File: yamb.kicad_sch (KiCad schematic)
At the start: 18 parts, among them J1 Barrel_Jack, J2 I2C, J3 HEADER, J4 HEADER_2.54, J5 Remote_Reset, J6 Power_Switch, P1 USB_C_Plug_USB2.0, SW1 RESET, U1 TPS3808DBV, U2 MCSBC, U3 SVR, U4 RAK4630, U5 BME280

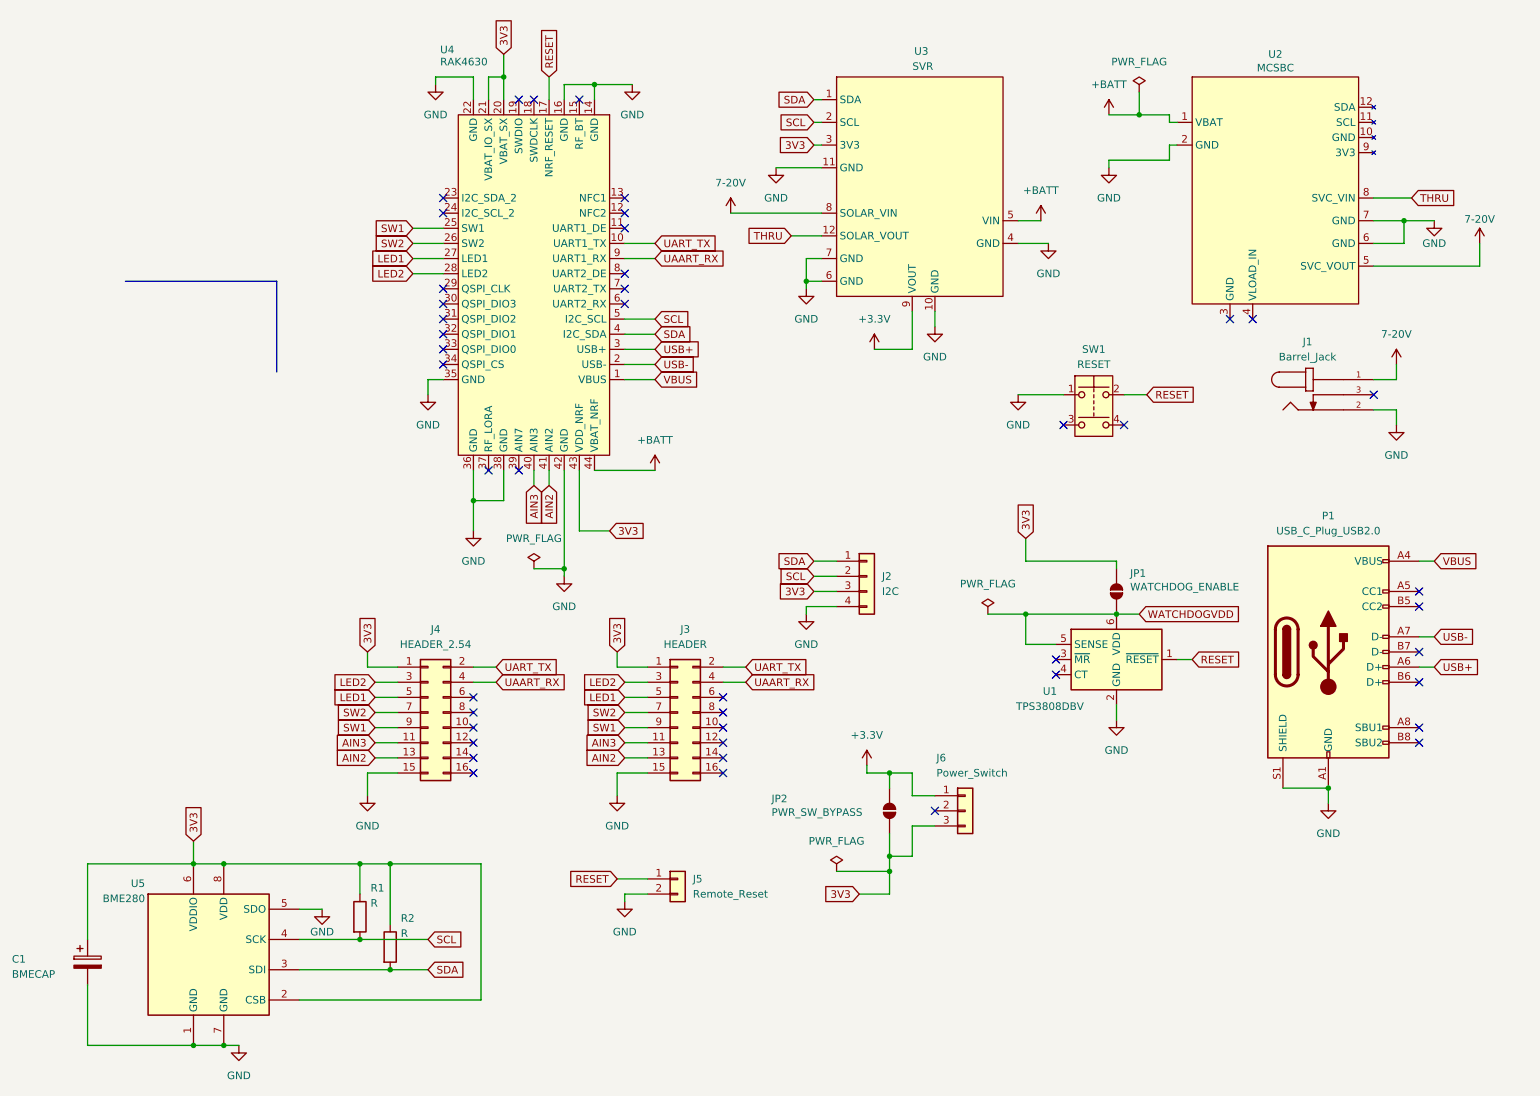
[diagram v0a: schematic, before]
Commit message: changed connectors to shroued 0.1" and cleaned some board DRC errors
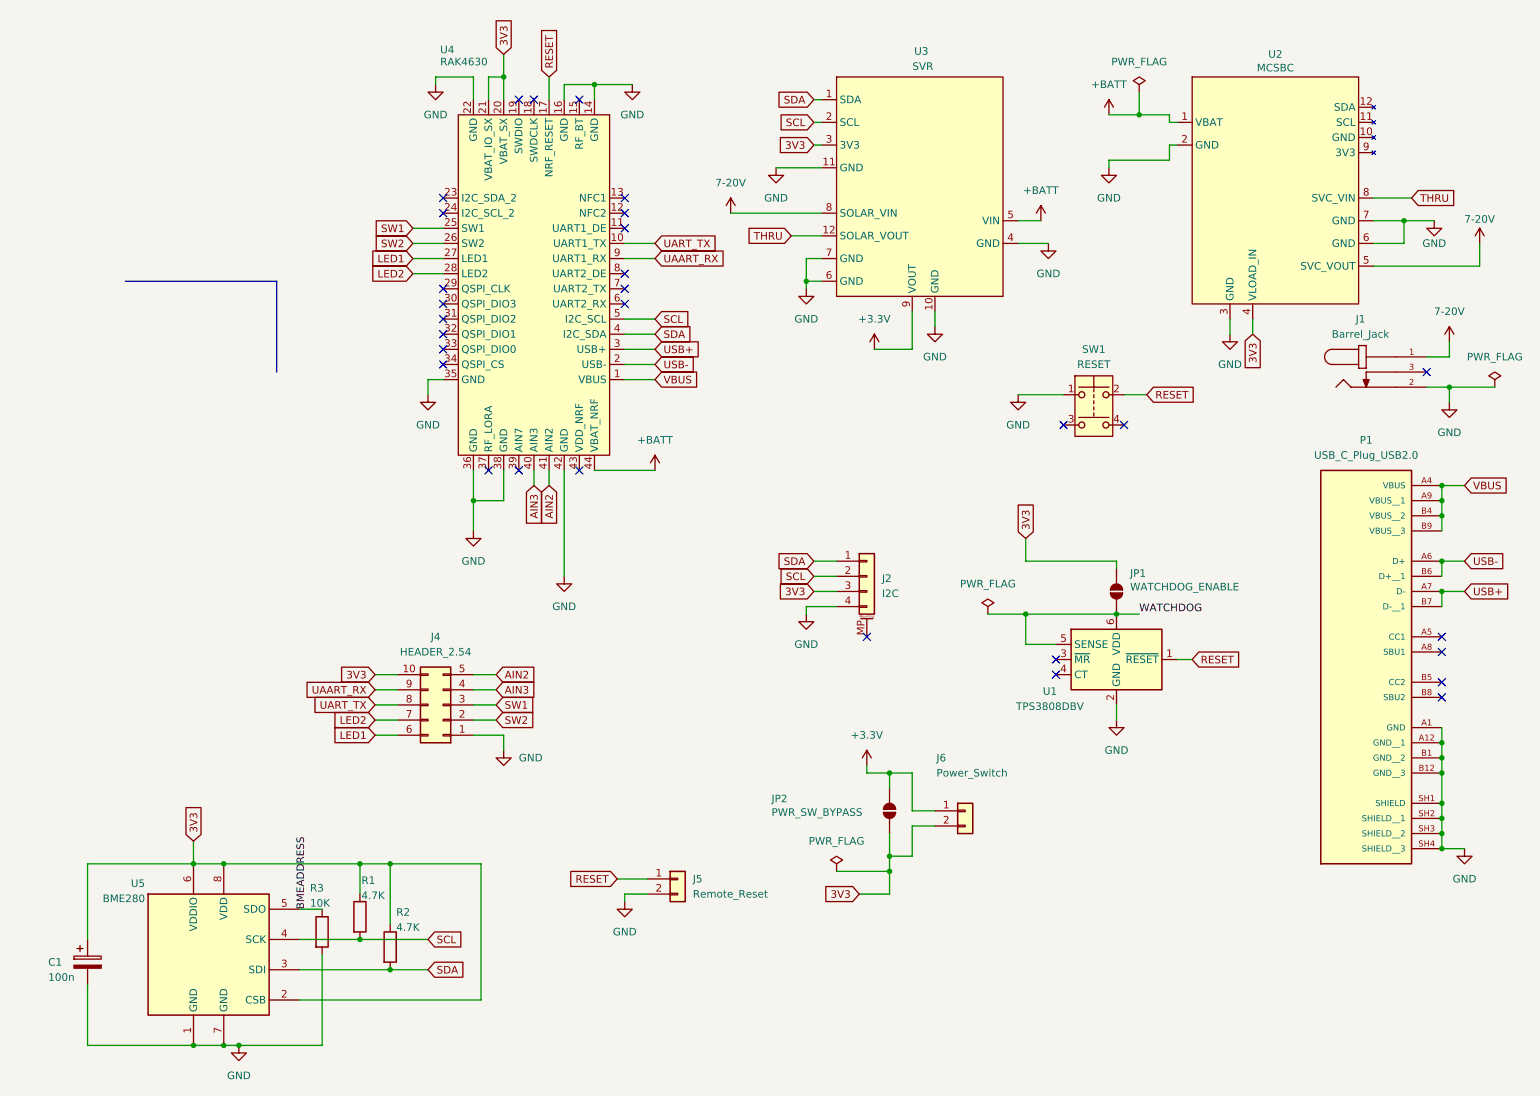
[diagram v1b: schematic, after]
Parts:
- removed J3: HEADER, Connector_JST:JST_PHD_B16B-PHDSS_2x08_P2.00mm_Vertical, symbol Connector_Generic:Conn_02x08_Odd_Even
- added R3: 10K, Resistor_SMD:R_1206_3216Metric_Pad1.30x1.75mm_HandSolder, symbol Device:R
- C1: value BMECAP -> 100n
- J2: footprint Connector_JST:JST_PH_B4B-PH-K_1x04_P2.00mm_Vertical -> Connector_JST:JST_SH_BM04B-SRSS-TB_1x04-1MP_P1.00mm_Vertical; symbol Connector_Generic:Conn_01x04 -> Connector_Generic_MountingPin:Conn_01x04_MountingPin
- J4: footprint Connector_PinHeader_2.54mm:PinHeader_2x08_P2.54mm_Vertical -> Andy_Footprints:CONN_7024610xx_MOL; symbol Connector_Generic:Conn_02x08_Odd_Even -> Connector_Generic:Conn_02x05_Top_Bottom
- J5: footprint Connector_PinHeader_1.00mm:PinHeader_1x02_P1.00mm_Vertical -> Andy_Footprints:CONN_SDA-70543-xxxx_02_MOL
- J6: footprint Connector_JST:JST_PH_B3B-PH-K_1x03_P2.00mm_Vertical -> Andy_Footprints:CONN_SDA-70543-xxxx_02_MOL; symbol Connector_Generic:Conn_01x03 -> Connector_Generic:Conn_01x02
- P1: footprint Connector_USB:USB_C_Receptacle_G-Switch_GT-USB-7051x -> Andy_Footprints:SAMESKY_UJ20-C-V-G-SMT-P16-TR; symbol Connector:USB_C_Receptacle_USB2.0_16P -> Andy_Symbols:UJ20-C-V-G-SMT-P16-TR; MANUFACTURER (none) -> Same Sky; MAXIMUM_PACKAGE_HEIGHT (none) -> 7.45mm; PARTREV (none) -> 1.0; STANDARD (none) -> Manufacturer Recommendations
- R1, R2: value R -> 4.7K
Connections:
- net 3V3: now also J4.10 (Pin_10), J6.2 (Pin_2), U2.4 (VLOAD_IN); no longer J4.1 (Pin_1), J6.3 (Pin_3), U4.43 (VDD_NRF)
- net AIN2: now also J4.5 (Pin_5); no longer J4.13 (Pin_13)
- net AIN3: now also J4.4 (Pin_4); no longer J4.11 (Pin_11)
- net GND: now also J4.1 (Pin_1), P1.SH1 (SHIELD), P1.SH2 (SHIELD__1), P1.SH3 (SHIELD__2), P1.SH4 (SHIELD__3), U2.3 (GND), R3.2; no longer J4.15 (Pin_15), P1.S1 (SHIELD), U5.5 (SDO)
- net LED1: now also J4.6 (Pin_6); no longer J4.5 (Pin_5)
- net LED2: now also J4.7 (Pin_7); no longer J4.3 (Pin_3)
- net SW1: now also J4.3 (Pin_3); no longer J4.9 (Pin_9)
- net SW2: now also J4.2 (Pin_2); no longer J4.7 (Pin_7)
- net UAART_RX: now also J4.9 (Pin_9); no longer J4.4 (Pin_4)
- net UART_TX: now also J4.8 (Pin_8); no longer J4.2 (Pin_2)
- net USB+: now also P1.A7 (D-), P1.B7 (D-__1); no longer P1.A6 (D+)
- net USB-: now also P1.A6 (D+), P1.B6 (D+__1); no longer P1.A7 (D-)
- net WATCHDOGVDD renamed WATCHDOG
- new net BMEADDRESS: R3.1, U5.5 (SDO)
- no-connect marks 45 -> 30
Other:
- moved on the sheet: J1
